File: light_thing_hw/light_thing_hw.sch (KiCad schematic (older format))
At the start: 60 parts, among them J1 CONNECTORS, J2 Li-Ion Battery, J3 ADDR_LED_PANEL_1_CONNECTORS, J4 ADDR_LED_PANEL_2_CONNECTORS, J5 MIC_CONN, Q1 MMBF170, Q2 BSS83P, SW1 ST_USER_BUTTON1, SW2 ST_RESET_BUTTON, U1 BC832-V1, U2 LSM6DS3, U3 MCP73833T-FCI_UN, U4 LMR62421XMF, U5 LP38511MRX-ADJ_NOPB, U6 STM32L476RGTx

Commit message: rev 3 work begun. changed battery connector, pulled down therm pin, broke out i2c1 pins. need to get a new accelerometer
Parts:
- removed TP1, TP2: TestPoint, TestPoint:TestPoint_Pad_D1.0mm, symbol Connector:TestPoint
- added J6: 3V3_TP, Connector_PinHeader_1.00mm:PinHeader_2x01_P1.00mm_Vertical, symbol Connector:Conn_01x02_Female
- added R19: 10k, Resistor_SMD:R_0603_1608Metric_Pad1.05x0.95mm_HandSolder, symbol Device:R
- J2: footprint Connector_Molex:Molex_PicoBlade_53261-0271_1x02-1MP_P1.25mm_Horizontal -> Connector_JST:JST_SH_BM02B-SRSS-TB_1x02-1MP_P1.00mm_Vertical
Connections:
- wire segments 205 -> 209
- no-connect marks 44 -> 42
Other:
- moved on the sheet: C13, C19, C20, C7, J1, J3, J4, J5, Q1, R10, R11, R12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

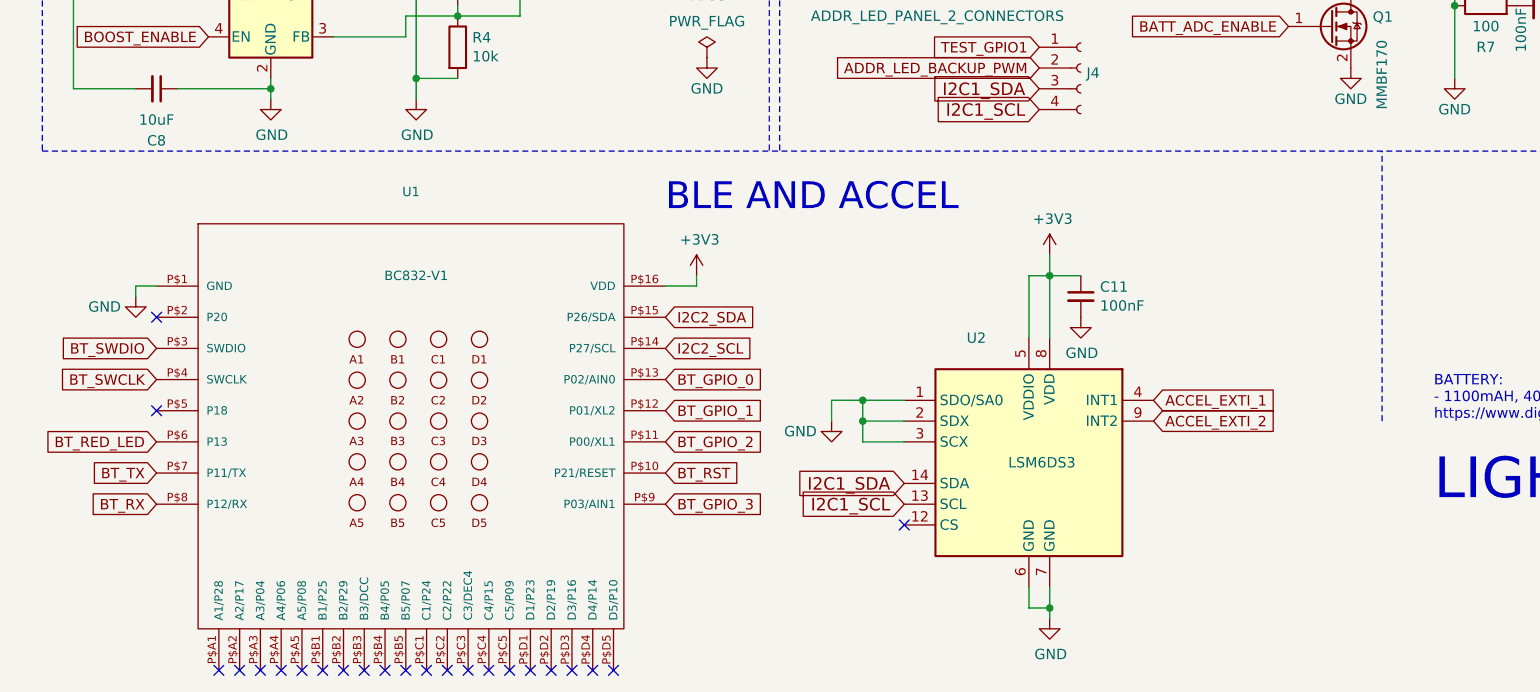
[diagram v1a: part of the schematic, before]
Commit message: using new accelerometer icm-20600
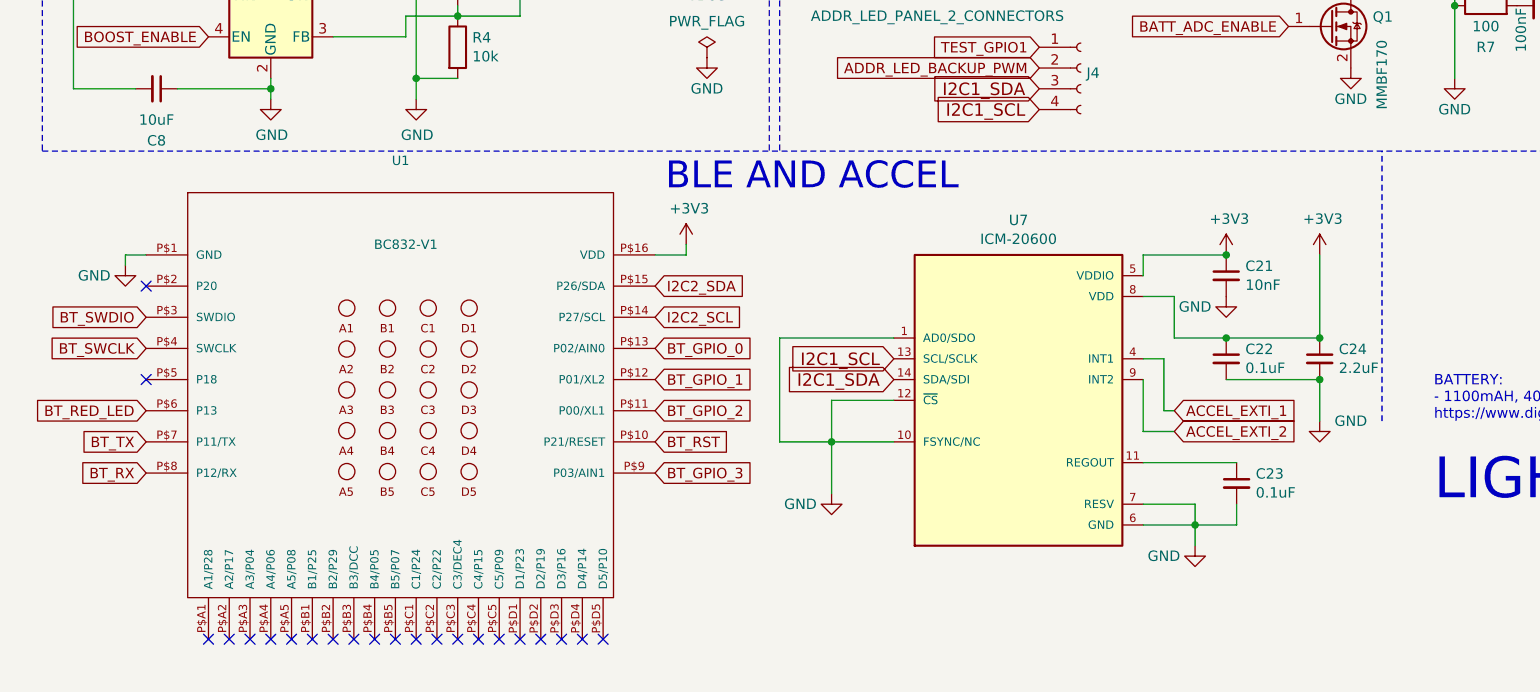
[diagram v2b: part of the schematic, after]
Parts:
- removed C11: 100nF, Capacitor_SMD:C_0603_1608Metric_Pad1.05x0.95mm_HandSolder, symbol Device:C_Small
- removed U2: LSM6DS3, footprints:LGA-14_3x2.5mm_P0.5mm_LayoutBorder3x4y_modded, symbol Sensor_Motion:LSM6DS3
- added C21: 10nF, Capacitor_SMD:C_0603_1608Metric_Pad1.05x0.95mm_HandSolder, symbol Device:C_Small
- added C22, C23: 0.1uF, Capacitor_SMD:C_0603_1608Metric_Pad1.05x0.95mm_HandSolder, symbol Device:C_Small
- added C24: 2.2uF, Capacitor_SMD:C_0603_1608Metric_Pad1.05x0.95mm_HandSolder, symbol Device:C_Small
- added U7: ICM-20600, ICM-20600:PQFN50P250X300X97-14N, symbol ICM-20600:ICM-20600
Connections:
- net +3V3: now also C21.1, C22.1, C24.1, U7.5 (VDDIO), U7.8 (VDD)
- net ACCEL_EXTI_1: now also U7.4 (INT1)
- net ACCEL_EXTI_2: now also U7.9 (INT2)
- net GND: now also C21.2, C22.2, C23.2, C24.2, U7.1 (AD0/SDO), U7.10 (FSYNC/NC), U7.12 (~CS), U7.6 (GND), U7.7 (RESV)
- net I2C1_SCL: now also U7.13 (SCL/SCLK)
- net I2C1_SDA: now also U7.14 (SDA/SDI)
- new net: C23.1, U7.11 (REGOUT)
- no-connect marks 42 -> 41
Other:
- moved on the sheet: U1

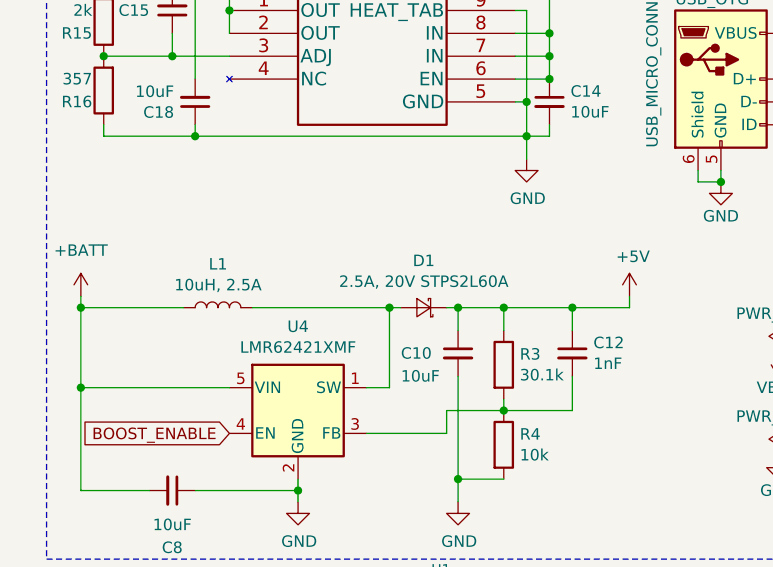
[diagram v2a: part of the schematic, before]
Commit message: changed the inductor footprint to something that will work
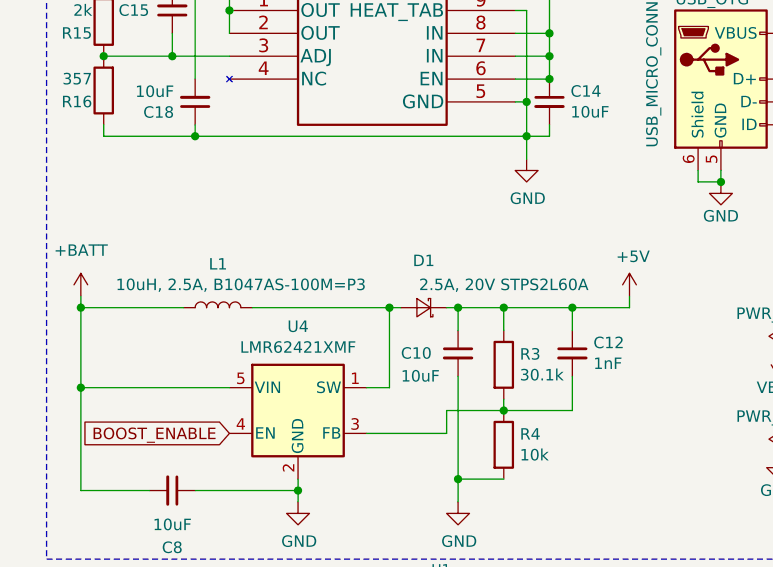
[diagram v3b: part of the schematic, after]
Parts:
- L1: value 10uH, 2.5A -> 10uH, 2.5A, B1047AS-100M=P3; footprint Inductor_SMD:L_0603_1608Metric_Pad1.05x0.95mm_HandSolder -> B1047AS_100M-P3_Inductor:IND_B1047AS-100M=P3
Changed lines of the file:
@@
 P 1250 4100
 F 0 "L1" V 1440 4100 50  0000 C CNN
-F 1 "10uH, 2.5A" V 1349 4100 50  0000 C CNN
-F 2 "Inductor_SMD:L_0603_1608Metric_Pad1.05x0.95mm_HandSolder" H 1250 4100 50  0001 C CNN
+F 1 "10uH, 2.5A, B1047AS-100M=P3" V 1350 4000 50  0000 C CNN
+F 2 "B1047AS_100M-P3_Inductor:IND_B1047AS-100M=P3" H 1250 4100 50  0001 C CNN
 F 3 "~" H 1250 4100 50  0001 C CNN
 	1    1250 4100
@@
 P 2150 4100
 F 0 "D1" H 2150 3895 50  0000 C CNN
-F 1 "2.5A, 20V  STPS2L60A" H 2150 3986 50  0000 C CNN
+F 1 "2.5A, 20V  STPS2L60A" H 1800 4000 50  0000 C CNN
 F 2 "Diode_SMD:D_SMA" V 2150 4100 50  0001 C CNN
 F 3 "~" V 2150 4100 50  0001 C CNN
